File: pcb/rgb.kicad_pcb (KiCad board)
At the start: 2 copper layers, 128 x 30 mm, 22 parts, among them J1 Conn_02x08_Odd_Even, J2 Conn_01x02, J3 Conn_01x02, P1 TTL_232R_3V3, U1 ESP-WROOM-32, U2 REG1117, U3 412D02F, U4 TACTILE, U5 TACTILE, U6 MicroSD_SPI_CD

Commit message: pcb: exploration
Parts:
- removed C5: 1u, Capacitors_SMD:C_0805
- removed J2: Conn_01x02, Pin_Headers:Pin_Header_Angled_1x02_Pitch2.54mm
- removed P1: TTL_232R_3V3, Pin_Headers:Pin_Header_Angled_1x06_Pitch2.54mm
- removed R4, R6: 10k, Resistors_SMD:R_0805
- removed REF** (x2): MountingHole_3.2mm_M3, Mounting_Holes:MountingHole_3.2mm_M3
- removed U3: 412D02F, myStuff:RPIA_SD_CARD
- removed U4: TACTILE, myStuff:EVQQ2
- removed U6: MicroSD_SPI_CD, newStuff:GCT-MEM2055-00-190-01-A
- added C10: 2u2, Capacitor_SMD:C_0603_1608Metric, F.Cu at (52.6, 116.3)
- added C11: 10u, Capacitor_SMD:C_1206_3216Metric, F.Cu at (80.2, 110.0)
- added C12: 2u2, Capacitor_SMD:C_0603_1608Metric, F.Cu at (83.0, 95.7)
- added C13: 2u2, Capacitor_SMD:C_0603_1608Metric, F.Cu at (85.5, 95.7)
- added C14: 10u, Capacitor_SMD:C_1206_3216Metric, F.Cu at (95.2, 100.2)
- added C15: 10u, Capacitor_SMD:C_1206_3216Metric, F.Cu at (95.2, 103.5)
- added C16: 10u, Capacitor_SMD:C_1206_3216Metric, F.Cu at (95.2, 106.9)
- added C17: 10u, Capacitor_SMD:C_1206_3216Metric, F.Cu at (95.2, 110.2)
- added C18: 10u, Capacitor_SMD:C_1206_3216Metric, F.Cu at (95.2, 82.0)
- added C19: 10u, Capacitor_SMD:C_1206_3216Metric, F.Cu at (95.2, 85.3)
- added C20: 10u, Capacitor_SMD:C_1206_3216Metric, F.Cu at (95.2, 88.7)
- added C21: 10u, Capacitor_SMD:C_1206_3216Metric, F.Cu at (95.2, 92.0)
- added C22: 2u2, Capacitor_SMD:C_0603_1608Metric, F.Cu at (83.7, 77.3)
- added C23: 2u2, Capacitor_SMD:C_0603_1608Metric, F.Cu at (86.2, 77.3)
- added C24: 10u, Capacitor_SMD:C_1206_3216Metric, F.Cu at (80.2, 82.0)
- added C25: 10u, Capacitor_SMD:C_1206_3216Metric, F.Cu at (80.2, 85.3)
- added C26: 10u, Capacitor_SMD:C_1206_3216Metric, F.Cu at (80.2, 88.7)
- added C27: 10u, Capacitor_SMD:C_1206_3216Metric, F.Cu at (80.2, 92.0)
- added C28: 2u2, Capacitor_SMD:C_0603_1608Metric, F.Cu at (88.0, 95.7)
- added C29: 2u2, Capacitor_SMD:C_0603_1608Metric, F.Cu at (88.7, 77.3)
- added C6: 2u2, Capacitor_SMD:C_0603_1608Metric, F.Cu at (52.6, 106.2)
- added C7: 2u2, Capacitor_SMD:C_0603_1608Metric, F.Cu at (52.6, 108.7)
- added C8: 2u2, Capacitor_SMD:C_0603_1608Metric, F.Cu at (52.6, 111.2)
- added C9: 2u2, Capacitor_SMD:C_0603_1608Metric, F.Cu at (52.6, 113.8)
- added J4: TYPE-C-31-M-12, Connector_USB:USB_C_Receptacle_GCT_USB4105-xx-A_16P_TopMnt_Horizontal, F.Cu at (98.2, 117.5)
- added J7: B4PS-VH, Connector_PinSocket_2.54mm:PinSocket_1x04_P2.54mm_Vertical, F.Cu at (99.8, 100.7)
- added L1: 3u3, Inductor_SMD:L_Sunlord_MWSA0503S, F.Cu at (87.8, 102.4)
- added L2: 3u3, Inductor_SMD:L_Sunlord_MWSA0503S, F.Cu at (88.6, 82.9)
- added R10: 57k, Resistor_SMD:R_0603_1608Metric, F.Cu at (56.6, 116.3)
- added R11: 10k, Resistor_SMD:R_0603_1608Metric, F.Cu at (60.6, 106.2)
- added R13: 22k, Resistor_SMD:R_0603_1608Metric, F.Cu at (60.6, 108.7)
- added R14: 22k, Resistor_SMD:R_0603_1608Metric, F.Cu at (60.6, 111.2)
- added R15: 1k37, Resistor_SMD:R_0603_1608Metric, F.Cu at (93.7, 77.3)
- added R5: 37k4, Resistor_SMD:R_0603_1608Metric, F.Cu at (56.6, 106.2)
- added R7: 22k, Resistor_SMD:R_0603_1608Metric, F.Cu at (56.6, 108.7)
- added R8: 1k, Resistor_SMD:R_0603_1608Metric, F.Cu at (56.6, 111.2)
- added R9: 10k, Resistor_SMD:R_0603_1608Metric, F.Cu at (56.6, 113.8)
- added U7: CH340C, Package_SO:SOIC-16_3.9x9.9mm_P1.27mm, F.Cu at (79.2, 117.5)
- added U8: SPX3819M5-L, Package_TO_SOT_SMD:SOT-23-5, F.Cu at (71.5, 78.2)
- C1: value 470n -> 10u; footprint Capacitors_SMD:C_0805 -> Capacitor_SMD:C_1206_3216Metric; moved to F.Cu
- C2, C3, C4: footprint Capacitors_SMD:C_0805 -> Capacitor_SMD:C_1206_3216Metric; moved to F.Cu
- J1: footprint Pin_Headers:Pin_Header_Angled_2x08_Pitch2.54mm -> Connector_PinSocket_2.54mm:PinSocket_2x08_P2.54mm_Vertical; moved to B.Cu
- J3: value Conn_01x02 -> B4PS-VH; footprint Pin_Headers:Pin_Header_Angled_1x02_Pitch2.54mm -> Connector_PinSocket_2.54mm:PinSocket_1x04_P2.54mm_Vertical
- R1: value 470k -> 10k; footprint Resistors_SMD:R_0805 -> Resistor_SMD:R_0603_1608Metric; moved to F.Cu
- R2: value 590R -> 1k37; footprint Resistors_SMD:R_0805 -> Resistor_SMD:R_0603_1608Metric; moved to F.Cu
- R3: value 1k -> 10k; footprint Resistors_SMD:R_0805 -> Resistor_SMD:R_0603_1608Metric; moved to F.Cu
- U1: value ESP-WROOM-32 -> SY8286ARAC; footprint myStuff:ESP-WROOM-32 -> Package_DFN_QFN:QFN-20-1EP_3x3mm_P0.45mm_EP1.6x1.6mm; moved to F.Cu
- U2: value REG1117 -> SY8286ARAC; footprint SOT-223 -> Package_DFN_QFN:QFN-20-1EP_3x3mm_P0.45mm_EP1.6x1.6mm; moved to F.Cu
- U5: value TACTILE -> ESP32-WROOM-32E; footprint myStuff:EVQQ2 -> RF_Module:ESP32-WROOM-32D; moved to F.Cu
- moved C3 108.7 mm to (80.2, 106.7), turned to 0 degrees
- moved U5 102.1 mm to (55.5, 86.9), turned to 90 degrees
- moved C2 99.2 mm to (80.2, 103.3), turned to 0 degrees
- moved R2 98.7 mm to (93.0, 95.7)
- moved R3 96.3 mm to (91.2, 77.3), turned to 90 degrees
- moved U2 93.8 mm to (87.5, 89.0), turned to 0 degrees
- moved J1 91.8 mm to (70.2, 91.5), turned to 180 degrees
- moved J3 85.6 mm to (99.8, 84.0), turned to 0 degrees
- moved C4 56.3 mm to (97.2, 95.8), turned to 0 degrees
- moved U1 49.0 mm to (87.5, 110.2)
- moved C1 44.0 mm to (80.2, 100.0), turned to 0 degrees
- moved R1 34.5 mm to (90.5, 95.7)
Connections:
- C1 pad 2: +3V3 -> VBUS
- C2 pad 2: +3V3 -> VBUS
- C3 pad 2: +5V -> VBUS
- J3 pad 1: +5V -> /Stepdown_b/v_out
- J3 pad 2: GND -> /Stepdown_b/v_out
- R1 pad 1: +3V3 -> +5V
- R1 pad 2: /rstBtn -> Net-(U1-FB)
- R2 pad 1: +3V3 -> Net-(U1-FB)
- R2 pad 2: Net-(R2-Pad2) -> GND
- R3 pad 1: Net-(R2-Pad2) -> /Stepdown_b/v_out
- R3 pad 2: GND -> Net-(U2-FB)
- U1 pad 1: GND -> Net-(C13-K)
- U1 pad 10: /OE -> unconnected-(U1-NC-Pad10)
- U1 pad 11: /STB -> VBUS
- U1 pad 12: /G1 -> GND
- U1 pad 13: /SD_CS -> unconnected-(U1-ILMT-Pad13)
- U1 pad 14: /SD_MISO -> Net-(U1-FB)
- U1 pad 15: GND -> Net-(C28-A)
- U1 pad 16: /B0 -> unconnected-(U1-NC-Pad16)
- U1 pad 18: Net-(U1-Pad18) -> GND
- U1 pad 19: Net-(U1-Pad19) -> Net-(C13-A)
- U1 pad 2: +3V3 -> VBUS
- U1 pad 20: Net-(U1-Pad20) -> Net-(C13-A)
- U1 pad 21: Net-(U1-Pad21) -> GND
- U1 pad 3: /rstBtn -> VBUS
- U1 pad 4: Net-(C5-Pad1) -> VBUS
- U1 pad 5: Net-(U1-Pad5) -> VBUS
- U1 pad 6: Net-(U1-Pad6) -> Net-(C13-A)
- U1 pad 7: Net-(U1-Pad7) -> GND
- U1 pad 8: /SD_MOSI -> GND
- U1 pad 9: /SD_CLK -> unconnected-(U1-PG-Pad9)
- U2 pad 1: Net-(R2-Pad2) -> Net-(C23-K)
- U2 pad 2: +3V3 -> VBUS
- U2 pad 3: +5V -> VBUS
- U2 pad 4: +3V3 -> VBUS
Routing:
- net +3V3: track 153.5 -> 0.00 mm, vias 3 -> 0
- net /rstBtn: track 98.5 -> 0.00 mm, vias 2 -> 0
- net /G1: track 78.0 -> 0.00 mm, vias 2 -> 0
- net /STB: track 56.5 -> 0.00 mm, vias 4 -> 0
- net /OE: track 54.0 -> 0.00 mm, vias 4 -> 0
- net /SD_MOSI: track 51.3 -> 0.00 mm
- net /SD_CS: track 48.5 -> 0.00 mm, vias 2 -> 0
- net /B0: track 43.6 -> 0.00 mm
- net /G0: track 42.2 -> 0.00 mm
- net /SD_CLK: track 41.1 -> 0.00 mm
- net Net-(P1-Pad4): track 40.5 -> 0.00 mm, vias 2 -> 0
- net GND: track 38.5 -> 0.00 mm, vias 15 -> 0
- net Net-(P1-Pad5): track 38.3 -> 0.00 mm, vias 2 -> 0
- net /SD_MISO: track 38.2 -> 0.00 mm
- net /R0: track 35.0 -> 0.00 mm
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- removed copper zone on B.Cu, net +3V3
- removed copper zone on B.Cu, net GND
- removed copper zone on F.Cu, net GND
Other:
- board size 128 x 30 mm -> 56 x 48 mm
- net class Default removed
- board text removed: "5V"
- board text removed: "Espirgbani"
- board text removed: "FLASH"
- board text removed: "LED panel"
- board text removed: "RESET"
- board text removed: "Rev 1, 02/2018"
- board text removed: "Sens"
- board text removed: "UART"

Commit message: initial routing done
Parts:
- removed R9: 10k, Resistor_SMD:R_0603_1608Metric
- added C5: 2u2, Capacitor_SMD:C_0603_1608Metric, F.Cu at (59.2, 102.8)
- added J2: Conn_01x02, Connector_PinHeader_2.54mm:PinHeader_1x02_P2.54mm_Horizontal, F.Cu at (48.2, 103.5)
- added J5: TF-01A, espirgbani:TF-01A, F.Cu at (53.5, 113.2)
- added R4: 10k, Resistor_SMD:R_0603_1608Metric, F.Cu at (54.5, 95.8)
- added R6: 10k, Resistor_SMD:R_0603_1608Metric, F.Cu at (59.2, 104.5)
- added U4: WIFI, espirgbani:EVQQ2, F.Cu at (73.8, 79.0)
- added U9: CH224K, espirgbani:SSOP-10-1EP_3.9x4.9mm_P1.00mm, F.Cu at (90.0, 119.3)
- L1, L2: value 3u3 -> SMDRH104R-4R7NT; footprint Inductor_SMD:L_Sunlord_MWSA0503S -> espirgbani:SMDRH104R-4R7NT
- moved C4 38.1 mm to (63.2, 113.0)
- moved C7 35.1 mm to (77.0, 83.5), turned to 180 degrees
- moved R14 34.5 mm to (64.5, 77.0), turned to 90 degrees
- moved C9 34.5 mm to (86.2, 121.0), turned to 90 degrees
- moved R15 33.8 mm to (93.0, 111.2), turned to 0 degrees
- moved C17 32.4 mm to (82.2, 80.6)
- moved R3 32.1 mm to (93.0, 109.4), turned to 180 degrees
- moved C8 31.9 mm to (78.0, 92.0), turned to -90 degrees
- moved C16 31.8 mm to (82.2, 77.8)
- moved R11 31.6 mm to (90.9, 115.0)
- moved R10 31.2 mm to (87.8, 115.0), turned to 180 degrees
- moved C29 30.6 mm to (93.0, 107.7), turned to 0 degrees
- moved C22 30.0 mm to (93.0, 105.9), turned to 0 degrees
- moved R8 29.6 mm to (84.5, 121.0), turned to 90 degrees
- moved C18 29.0 mm to (82.2, 107.9)
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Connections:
- C4 pad 1: +3V3 -> +3.3V
- U5 pad 14: unconnected-(U5-IO12-Pad14) -> /CLK
- U5 pad 29: /A -> /B
- U5 pad 30: /B -> /A
- U5 pad 36: /CLK -> unconnected-(U5-IO22-Pad36)
- U7 pad 5: /USB_D_P -> /USB_P
- U7 pad 6: /USB_D_N -> /USB_N
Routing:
- net +3.3V: track 0.00 -> 93.1 mm, vias 0 -> 9
- net /pd_bad: track 0.00 -> 76.3 mm, vias 0 -> 4
- net /esp_tx: track 0.00 -> 64.3 mm, vias 0 -> 4
- net /esp_rx: track 0.00 -> 61.9 mm, vias 0 -> 4
- net /D: track 0.00 -> 52.4 mm, vias 0 -> 3
- net /C: track 0.00 -> 46.5 mm, vias 0 -> 3
- net /esp_prog: track 0.00 -> 44.3 mm, vias 0 -> 4
- net /esp_reset: track 0.00 -> 43.1 mm, vias 0 -> 4
- net Net-(U5-IO34): track 0.00 -> 42.0 mm, vias 0 -> 5
- net VBUS: track 0.00 -> 41.9 mm, vias 0 -> 7
- net /B: track 0.00 -> 40.3 mm, vias 0 -> 3
- net /A: track 0.00 -> 39.5 mm, vias 0 -> 3
- net /B1: track 0.00 -> 35.2 mm, vias 0 -> 3
- net /R1: track 0.00 -> 31.2 mm, vias 0 -> 1
- net /OE: track 0.00 -> 29.7 mm, vias 0 -> 1
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- added copper zone on F.Cu, net +5V
- added copper zone on F.Cu, net /Stepdown_b/v_out
- added copper zone on B.Cu, net GND
- added copper zone on F.Cu, net GND
- added copper zone on In1.Cu, net GND
- added copper zone on In2.Cu, net GND
- added copper zone on F.Cu, net Net-(C13-A)
- added copper zone on F.Cu, net Net-(C23-A)
- added copper zone on F.Cu, net VBUS
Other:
- board size 56 x 48 mm -> 58 x 48 mm
- copper layers 2 -> 4
- rule pad_to_mask_clearance: 0.2 -> 0

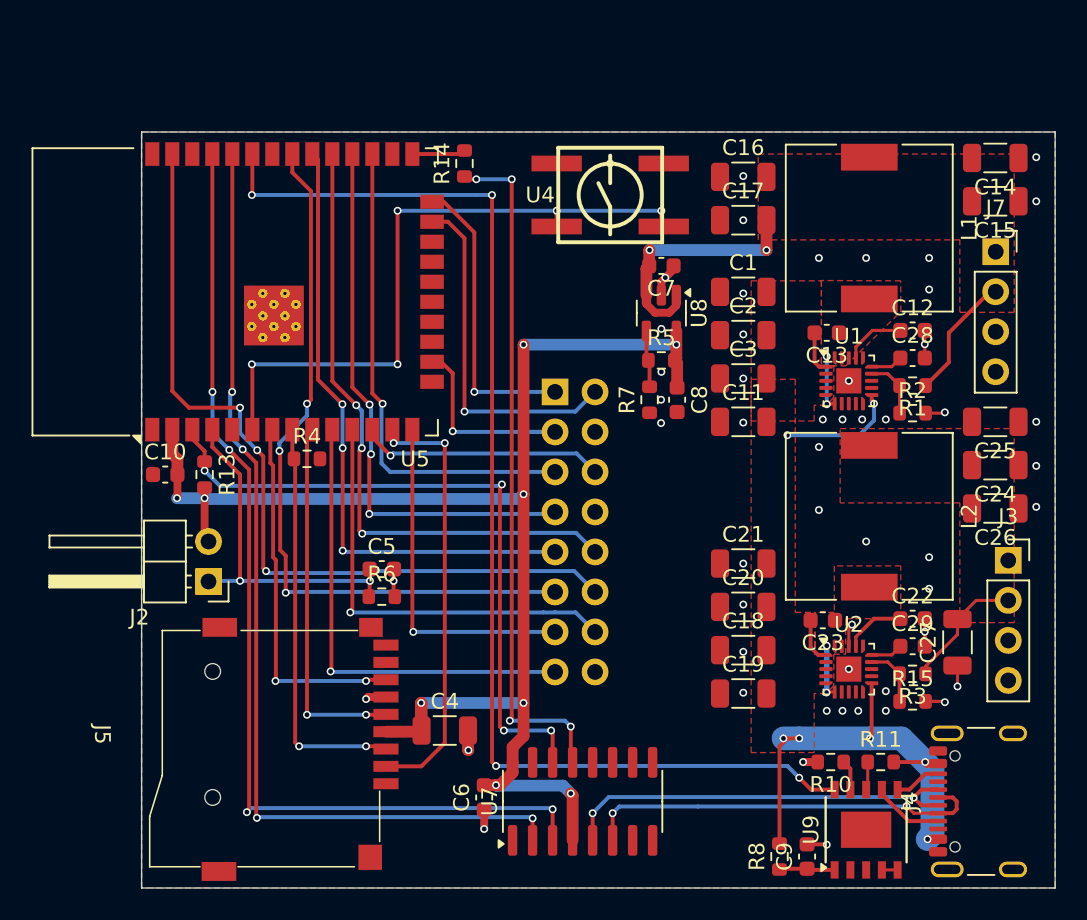
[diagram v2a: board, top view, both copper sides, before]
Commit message: turn esp by 90 deg
rip-up, re-route
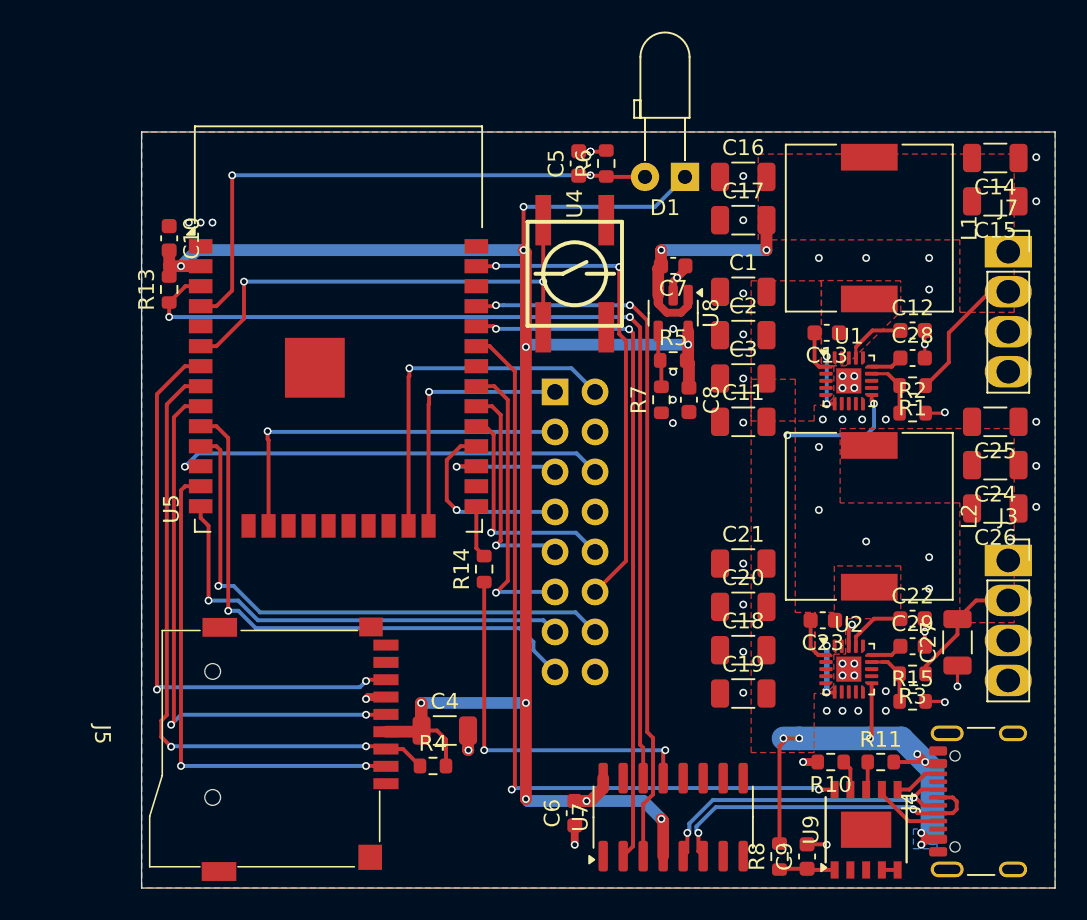
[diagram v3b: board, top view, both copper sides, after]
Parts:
- removed J2: Conn_01x02, Connector_PinHeader_2.54mm:PinHeader_1x02_P2.54mm_Horizontal
- added D1: ALS-PDIC144-6C/L378, LED_THT:LED_D3.0mm_Horizontal_O3.81mm_Z6.0mm, F.Cu at (78.5, 77.8)
- moved R6 31.0 mm to (73.5, 77.0), turned to 90 degrees
- moved C5 28.6 mm to (71.8, 77.0), turned to 90 degrees
- moved R14 25.8 mm to (65.8, 102.8)
- moved R4 21.1 mm to (62.5, 115.2)
- moved C10 15.0 mm to (45.8, 81.8), turned to -90 degrees
- moved R13 12.0 mm to (45.8, 85.0), turned to 90 degrees
- moved U5 6.43 mm to (56.5, 90.5), turned to 0 degrees
- moved C6 5.84 mm to (71.5, 118.2)
- moved U7 5.84 mm to (77.8, 118.5)
- moved U4 5.48 mm to (71.5, 84.0), turned to 90 degrees
- moved J7 0.80 mm to (99.0, 82.6)
- moved C7 0.75 mm to (77.8, 83.5)
- moved C8 0.75 mm to (78.8, 92.0)
- moved R5 0.75 mm to (77.8, 89.5)
- moved R7 0.75 mm to (77.0, 92.0)
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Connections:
- R4 pad 2: +3V3 -> +3.3V
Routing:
- net /C: track 46.5 -> 18.7 mm, vias 3 -> 1
- net /pd_bad: track 76.3 -> 50.3 mm, vias 4 -> 2
- net /B: track 40.3 -> 14.7 mm, vias 3 -> 1
- net /A: track 39.5 -> 14.1 mm, vias 3 -> 1
- net +3.3V: track 93.1 -> 118.3 mm, vias 9 -> 10
- net /R1: track 31.2 -> 7.65 mm
- net /B1: track 35.2 -> 12.0 mm, vias 3 -> 1
- net /D: track 52.4 -> 30.7 mm, vias 3 -> 2
- net /esp_prog: track 44.3 -> 24.0 mm, vias 4 -> 2
- net /esp_reset: track 43.1 -> 62.2 mm, vias 4 -> 2
- net /esp_tx: track 64.3 -> 45.7 mm, vias 4 -> 2
- net /esp_rx: track 61.9 -> 43.6 mm, vias 4 -> 2
- net /SD_MOSI: track 25.9 -> 41.1 mm
- net Net-(D1-A): track 22.4 -> 36.6 mm
- net /SD_MISO: track 23.2 -> 37.1 mm
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- added copper zone on B.Cu, net VBUS

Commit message: optimize pinout
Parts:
- C4: value 10u -> 2u2; footprint Capacitor_SMD:C_1206_3216Metric -> Capacitor_SMD:C_0603_1608Metric
- moved R4 30.7 mm to (45.8, 89.5), turned to 90 degrees
- moved C4 14.8 mm to (52.8, 102.5), turned to 180 degrees
- moved J5 2.79 mm to (54.0, 110.5), turned to 0 degrees
- moved C10 0.75 mm to (45.8, 82.5)
- moved R13 0.75 mm to (45.8, 85.8)
- moved R14 0.25 mm to (65.5, 102.8)
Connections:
- U5 pad 10: /OE -> /SD_MISO
- U5 pad 11: /STB -> /SD_CLK
- U5 pad 12: /G1 -> /SD_MOSI
- U5 pad 14: /CLK -> /OE
- U5 pad 16: /B0 -> /CLK
- U5 pad 23: /G0 -> /STB
- U5 pad 24: /R0 -> /C
- U5 pad 26: unconnected-(U5-IO4-Pad26) -> /D
- U5 pad 27: /R1 -> /A
- U5 pad 28: /B1 -> /B
- U5 pad 29: /B -> /B1
- U5 pad 30: /A -> /R1
- U5 pad 31: /C -> /G1
- U5 pad 33: /pd_bad -> /B0
- U5 pad 36: unconnected-(U5-IO22-Pad36) -> /R0
- U5 pad 37: /D -> /G0
- U5 pad 7: /SD_MISO -> unconnected-(U5-IO35-Pad7)
- U5 pad 8: /SD_MOSI -> unconnected-(U5-IO32-Pad8)
- U5 pad 9: /SD_CLK -> unconnected-(U5-IO33-Pad9)
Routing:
- net /SD_MISO: track 37.1 -> 0.00 mm, vias 2 -> 0
- net /SD_CLK: track 35.5 -> 0.00 mm, vias 2 -> 0
- net /SD_CS: track 31.9 -> 0.00 mm, vias 2 -> 0
- net /SD_MOSI: track 41.1 -> 9.49 mm, vias 2 -> 0
- net /pd_bad: track 50.3 -> 20.8 mm
- net /STB: track 35.2 -> 17.1 mm
- net /D: track 30.7 -> 13.0 mm, vias 2 -> 1
- net /G1: track 27.9 -> 11.6 mm
- net /B0: track 24.3 -> 9.66 mm
- net /CLK: track 29.0 -> 19.8 mm, vias 1 -> 0
- net +3.3V: track 118.3 -> 110.1 mm, vias 10 -> 8
- net /G0: track 22.4 -> 15.1 mm, vias 1 -> 2
- net /C: track 18.7 -> 12.0 mm
- net /OE: track 35.7 -> 29.2 mm
- net /R0: track 16.5 -> 12.0 mm, vias 1 -> 2
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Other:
- outline, holes or cut-outs redrawn

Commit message: finish routing
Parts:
- moved C4 1.74 mm to (54.5, 102.2), turned to 0 degrees
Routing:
- net /SD_CLK: track 0.00 -> 26.2 mm, vias 0 -> 4
- net /SD_CS: track 0.00 -> 24.9 mm, vias 0 -> 2
- net /SD_MOSI: track 9.49 -> 33.5 mm, vias 0 -> 4
- net +3.3V: track 110.1 -> 126.0 mm, vias 8 -> 10
- net /SD_MISO: track 0.00 -> 12.7 mm
- net /OE: track 29.2 -> 35.3 mm
- net /CLK: track 19.8 -> 24.9 mm, vias 0 -> 3
- net /STB: track 17.1 -> 18.5 mm
- net GND: track 16.2 -> 17.0 mm, vias 60 -> 76
- net Net-(D1-A): track 36.2 -> 36.1 mm, vias 3 -> 2
- removed copper zone on In1.Cu, net GND
- removed copper zone on In2.Cu, net GND
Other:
- copper layers 4 -> 2
